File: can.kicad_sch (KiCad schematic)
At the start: 12 parts, among them J400 Conn_01x04_Pin, U400 TJA1042T-3

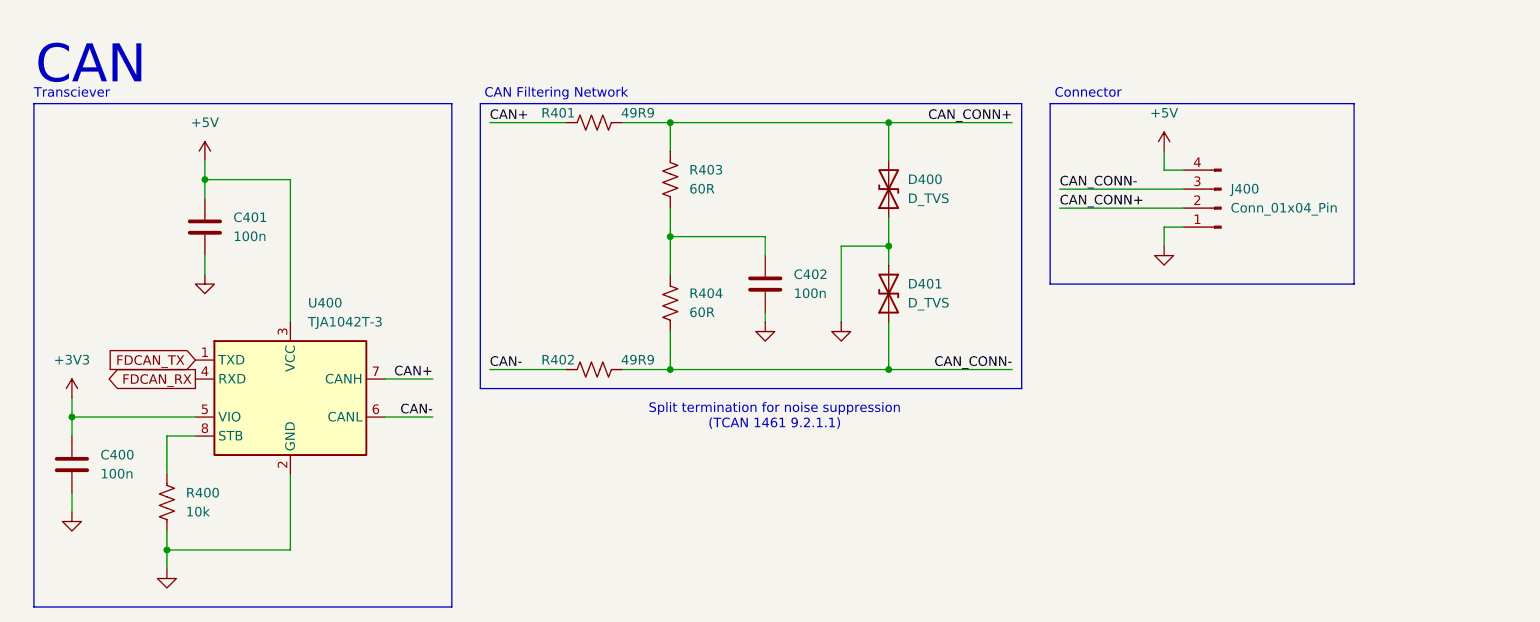
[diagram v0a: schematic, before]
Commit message: Footprints added
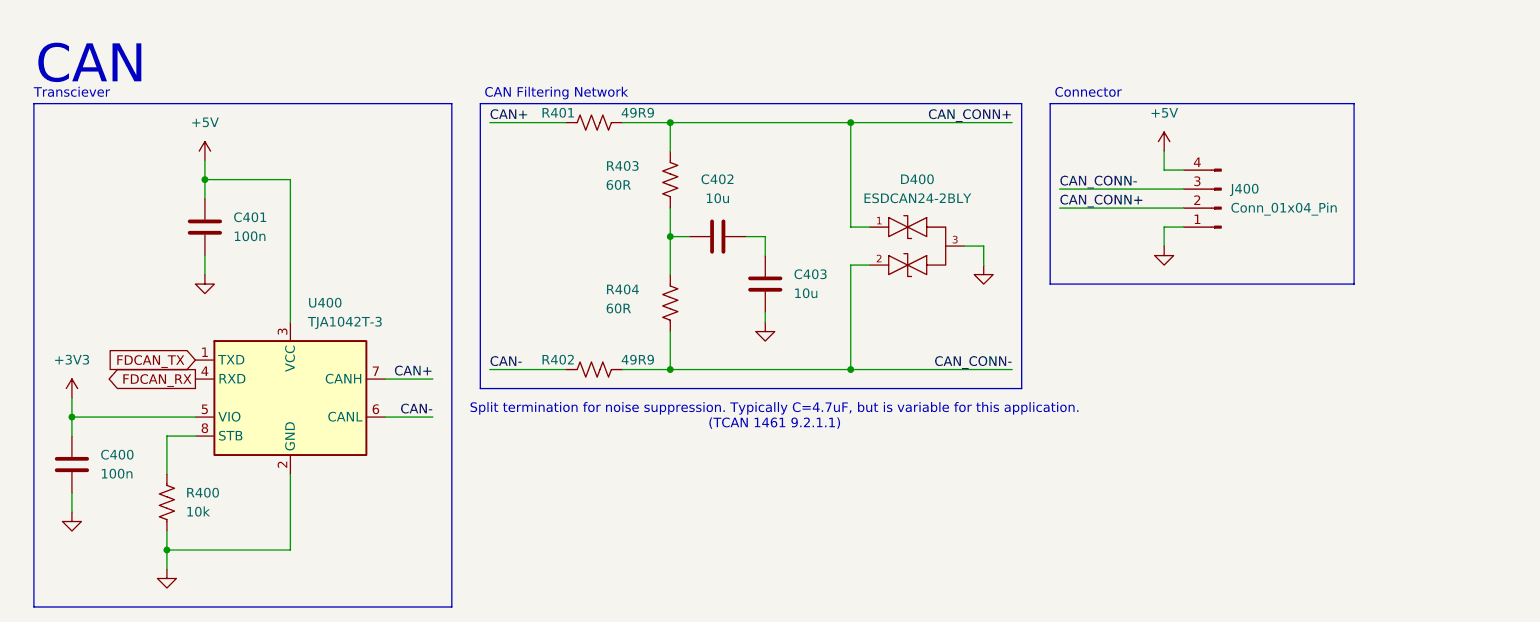
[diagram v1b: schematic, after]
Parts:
- removed D400, D401: D_TVS, symbol Device:D_TVS
- added C403: 10u, Capacitor_SMD:C_0201_0603Metric, symbol Device:C
- added D400: ESDCAN24-2BLY, Package_TO_SOT_SMD:SOT-23-3, symbol lcsc:ESDCAN24-2BLY
- C400, C401: footprint (none) -> Capacitor_SMD:C_01005_0402Metric
- C402: value 100n -> 10u; footprint (none) -> Capacitor_SMD:C_0201_0603Metric
- J400: footprint (none) -> Connector_PinHeader_2.54mm:PinHeader_1x04_P2.54mm_Vertical
- R400, R401, R402, R403, R404: footprint (none) -> Resistor_SMD:R_01005_0402Metric
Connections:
- net CAN_CONN+: now also D400.1
- net CAN_CONN-: now also D400.2
- net GND: now also C403.1, D400.3; no longer C402.2
- new net: C402.2, C403.2
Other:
- note added: "Split termination for noise suppression. Typically C=4.7uF, but is variable for this application. (TCAN 1461 9.2.1.1)"
- note removed: "Split termination for noise suppression (TCAN 1461 9.2.1.1)"
- moved on the sheet: C402

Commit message: Some changes to power circuitry, more layout
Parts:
- C400, C401: footprint Capacitor_SMD:C_01005_0402Metric -> Capacitor_SMD:C_0402_1005Metric
- C402, C403: footprint Capacitor_SMD:C_0201_0603Metric -> Capacitor_SMD:C_0603_1608Metric
- R400, R401, R402, R403, R404: footprint Resistor_SMD:R_01005_0402Metric -> Resistor_SMD:R_0402_1005Metric
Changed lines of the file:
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@@
 			)
 		)
-		(property "Footprint" "Capacitor_SMD:C_01005_0402Metric"
+		(property "Footprint" "Capacitor_SMD:C_0402_1005Metric"
 			(at 41.6052 44.45 0)
 			(effects
@@
 			)
 		)
-		(property "Footprint" "Resistor_SMD:R_01005_0402Metric"
+		(property "Footprint" "Resistor_SMD:R_0402_1005Metric"
 			(at 36.576 77.724 90)
 			(effects
@@
 			)
 		)
-		(property "Footprint" "Resistor_SMD:R_01005_0402Metric"
+		(property "Footprint" "Resistor_SMD:R_0402_1005Metric"
 			(at 103.886 51.054 90)
 			(effects
@@
 			)
 		)
-		(property "Footprint" "Resistor_SMD:R_01005_0402Metric"
+		(property "Footprint" "Resistor_SMD:R_0402_1005Metric"
 			(at 92.964 58.674 90)
 			(effects
@@
 			)
 		)
-		(property "Footprint" "Resistor_SMD:R_01005_0402Metric"
+		(property "Footprint" "Resistor_SMD:R_0402_1005Metric"
 			(at 92.964 25.654 90)
 			(effects
@@
 			)
 		)
-		(property "Footprint" "Capacitor_SMD:C_0201_0603Metric"
+		(property "Footprint" "Capacitor_SMD:C_0603_1608Metric"
 			(at 113.03 40.9448 0)
 			(effects
@@
 			)
 		)
-		(property "Footprint" "Capacitor_SMD:C_01005_0402Metric"
+		(property "Footprint" "Capacitor_SMD:C_0402_1005Metric"
 			(at 23.8252 76.2 0)
 			(effects
@@
 			)
 		)
-		(property "Footprint" "Capacitor_SMD:C_0201_0603Metric"
+		(property "Footprint" "Capacitor_SMD:C_0603_1608Metric"
 			(at 114.6048 44.45 0)
 			(effects
@@
 			)
 		)
-		(property "Footprint" "Resistor_SMD:R_01005_0402Metric"
+		(property "Footprint" "Resistor_SMD:R_0402_1005Metric"
 			(at 103.886 34.544 90)
 			(effects

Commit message: I hate everything
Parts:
- removed J400: Conn_01x04_Pin, Connector_PinHeader_2.54mm:PinHeader_1x04_P2.54mm_Vertical, symbol Connector:Conn_01x04_Pin
- removed R400: 10k, Resistor_SMD:R_0402_1005Metric, symbol Device:R_US
- added J102: Conn_01x03, Connector_PinHeader_2.54mm:PinHeader_1x03_P2.54mm_Vertical, symbol Connector_Generic:Conn_01x03
- added JP400: Jumper_2_Bridged, Connector_PinHeader_2.54mm:PinHeader_1x02_P2.54mm_Vertical, symbol Jumper:Jumper_2_Bridged
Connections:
- net CAN_CONN+: now also J102.2 (Pin_2)
- net CAN_CONN-: now also J102.1 (Pin_1)
- net GND: now also J102.3 (Pin_3), JP400.2 (B); no longer C403.1
- net STDBY: now reaches U400.8 (STB)
- new net: C403.1, JP400.1 (A)
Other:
- moved on the sheet: C403, D400

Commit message: First workable layout
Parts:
- C400, C401: LCSC (none) -> C1525
- C402, C403: LCSC (none) -> C19702
- J102, JP400: LCSC (none) -> C2337
- R401, R402: LCSC (none) -> C87044
- R403, R404: LCSC (none) -> C137954
- U400: LCSC (none) -> C22445414
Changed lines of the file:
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@@
 	(title_block
 		(title "Thermocouple Board")
-		(date "2025-10-07")
+		(date "2025-10-09")
 		(rev "1A")
 		(company "Aggie Propulsion and Rocketry Lab")
@@
 			)
 		)
+		(property "LCSC" "C1525"
+			(at 44.45 39.3699 0)
+			(effects
+				(font
+					(size 1.27 1.27)
+				)
+				(hide yes)
+			)
+		)
 		(pin "2"
 		)
@@
 			)
 		)
+		(property "LCSC" "C2337"
+			(at 132.08 36.83 0)
+			(effects
+				(font
+					(size 1.27 1.27)
+				)
+				(hide yes)
+			)
+		)
 		(pin "1"
 		)
@@
 		(property "Description" "Resistor, US symbol"
 			(at 102.87 50.8 0)
+			(effects
+				(font
+					(size 1.27 1.27)
+				)
+				(hide yes)
+			)
+		)
+		(property "LCSC" "C137954"
+			(at 94.234 49.022 0)
 			(effects
 				(font
@@
 			)
 		)
+		(property "LCSC" "C2337"
+			(at 203.2 34.2899 0)
+			(effects
+				(font
+					(size 1.27 1.27)
+				)
+				(hide yes)
+			)
+		)
 		(pin "1"
 		)
@@
 			)
 		)
+		(property "LCSC" "C87044"
+			(at 87.884 58.42 0)
+			(effects
+				(font
+					(size 1.27 1.27)
+				)
+				(hide yes)
+			)
+		)
 		(pin "1"
 		)
@@
 		(property "Description" "Resistor, US symbol"
 			(at 92.71 26.67 0)
+			(effects
+				(font
+					(size 1.27 1.27)
+				)
+				(hide yes)
+			)
+		)
+		(property "LCSC" "C87044"
+			(at 87.884 25.4 0)
 			(effects
 				(font
@@
 			)
 		)
+		(property "LCSC" "C22445414"
+			(at 54.4195 50.8 0)
+			(effects
+				(font
+					(size 1.27 1.27)
+				)
+				(hide yes)
+			)
+		)
 		(pin "1"
 		)
@@
 			)
 		)
+		(property "LCSC" "C19702"
+			(at 109.22 34.29 0)
+			(effects
+				(font
+					(size 1.27 1.27)
+				)
+				(hide yes)
+			)
+		)
 		(pin "2"
 		)
@@
 			)
 		)
+		(property "LCSC" "C1525"
+			(at 26.67 71.1199 0)
+			(effects
+				(font
+					(size 1.27 1.27)
+				)
+				(hide yes)
+			)
+		)
 		(pin "2"
 		)
@@
 			)
 		)
+		(property "LCSC" "C19702"
+			(at 119.38 34.29 0)
+			(effects
+				(font
+					(size 1.27 1.27)
+				)
+				(hide yes)
+			)
+		)
 		(pin "2"
 		)
@@
 			(effects
 				(font
+					(size 1.27 1.27)
+				)
+				(hide yes)
+			)
+		)
+		(property "LCSC" "C137954"
+			(at 94.234 32.512 0)
+			(effects
+				(font

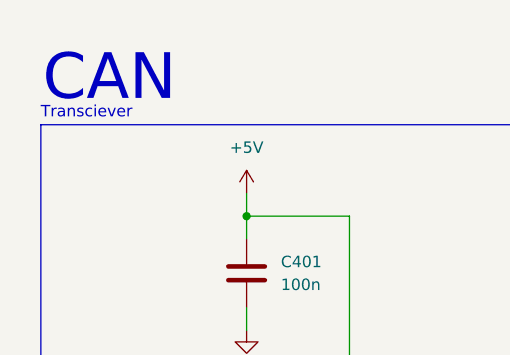
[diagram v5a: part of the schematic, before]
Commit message: Modify repo for usage on Linux, add basic CI
chore: fix CI

Small things
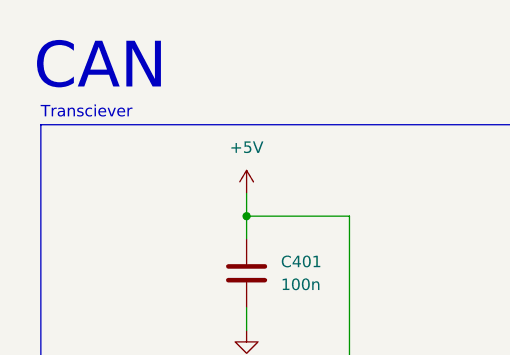
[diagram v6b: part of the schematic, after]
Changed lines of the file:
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@@
 	(text "CAN"
 		(exclude_from_sim no)
-		(at 25.4 19.05 0)
+		(at 24.384 17.78 0)
 		(effects
 			(font
